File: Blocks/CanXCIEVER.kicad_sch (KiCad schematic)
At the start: 2 parts, among them IC45 TCAN337DCNR, J5 TC0203620000G

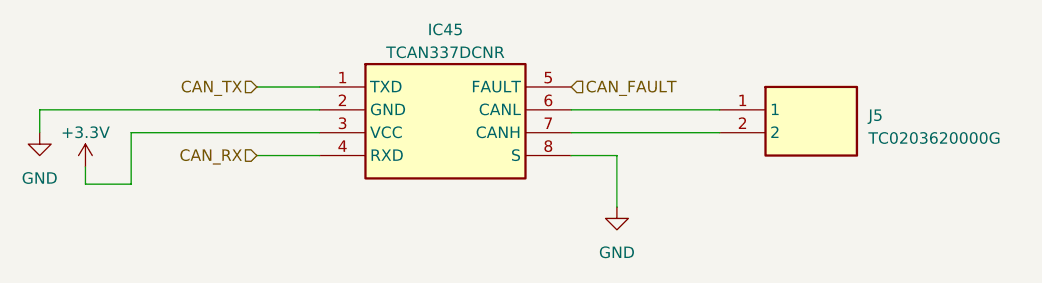
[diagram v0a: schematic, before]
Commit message: Automate library addition * Added script to automagically extract samacsys libraries and put them in corresponding folders. * Note: Requires zsh
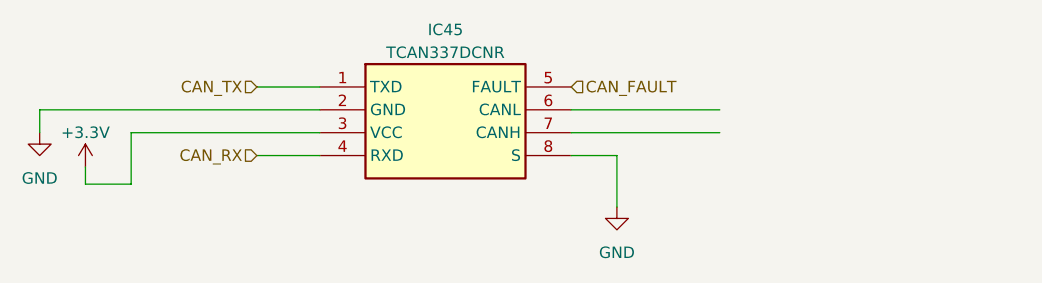
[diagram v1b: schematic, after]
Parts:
- removed J5: TC0203620000G, TC0203620000G:TC0203620000G, symbol TC0203620000G:TC0203620000G
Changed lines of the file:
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@@
   (symbol (lib_id "power:+3.3V") (at 98.425 107.95 0) (unit 1)
     (in_bom yes) (on_board yes) (dnp no) (fields_autoplaced)
-    (property "Reference" "#PWR0117" (at 98.425 111.76 0)
+    (property "Reference" "#PWR0284" (at 98.425 111.76 0)
       (effects (font (size 1.27 1.27)) hide)
     )
@@
       (project "PLC-CIM"
         (path "/98f81d77-8880-491b-a7cf-4c27e2d73edf/a733259a-e36e-4b53-aba1-6642256ff9ff"
-          (reference "#PWR0117") (unit 1)
+          (reference "#PWR0284") (unit 1)
         )
       )
@@
   (symbol (lib_id "power:GND") (at 157.48 112.395 0) (unit 1)
     (in_bom yes) (on_board yes) (dnp no) (fields_autoplaced)
-    (property "Reference" "#PWR0124" (at 157.48 118.745 0)
+    (property "Reference" "#PWR0283" (at 157.48 118.745 0)
       (effects (font (size 1.27 1.27)) hide)
     )
@@
       (project "PLC-CIM"
         (path "/98f81d77-8880-491b-a7cf-4c27e2d73edf/a733259a-e36e-4b53-aba1-6642256ff9ff"
-          (reference "#PWR0124") (unit 1)
+          (reference "#PWR0283") (unit 1)
         )
       )
@@
     )
   )
-  (symbol (lib_id "TC0203620000G:TC0203620000G") (at 168.91 101.6 0) (unit 1)
-    (in_bom yes) (on_board yes) (dnp no) (fields_autoplaced)
-    (property "Reference" "J5" (at 185.42 102.235 0)
-      (effects (font (size 1.27 1.27)) (justify left))
-    )
-    (property "Value" "TC0203620000G" (at 185.42 104.775 0)
-      (effects (font (size 1.27 1.27)) (justify left))
-    )
-    (property "Footprint" "TC0203620000G:TC0203620000G" (at 185.42 196.52 0)
-      (effects (font (size 1.27 1.27)) (justify left top) hide)
-    )
-    (property "Datasheet" "https://componentsearchengine.com/Datasheets/1/TC0203620000G.pdf" (at 185.42 296.52 0)
-      (effects (font (size 1.27 1.27)) (justify left top) hide)
-    )
-    (property "Height" "10.5" (at 185.42 496.52 0)
-      (effects (font (size 1.27 1.27)) (justify left top) hide)
-    )
-    (property "Mouser Part Number" "649-TC02036200J0G" (at 185.42 596.52 0)
-      (effects (font (size 1.27 1.27)) (justify left top) hide)
-    )
-    (property "Mouser Price/Stock" "https://www.mouser.co.uk/ProductDetail/Amphenol-Anytek/TC0203620000G?qs=Mv7BduZupUiHURQaUHJ1XQ%3D%3D" (at 185.42 696.52 0)
-      (effects (font (size 1.27 1.27)) (justify left top) hide)
-    )
-    (property "Manufacturer_Name" "Amphenol" (at 185.42 796.52 0)
-      (effects (font (size 1.27 1.27)) (justify left top) hide)
-    )
-    (property "Manufacturer_Part_Number" "TC0203620000G" (at 185.42 896.52 0)
-      (effects (font (size 1.27 1.27)) (justify left top) hide)
-    )
-    (pin "1")
-    (pin "2")
-    (instances
-      (project "PLC-CIM"
-        (path "/98f81d77-8880-491b-a7cf-4c27e2d73edf"
-          (reference "J5") (unit 1)
-        )
-        (path "/98f81d77-8880-491b-a7cf-4c27e2d73edf/65732d30-4757-4d69-a8f8-277854263560"
-          (reference "J6") (unit 1)
-        )
-        (path "/98f81d77-8880-491b-a7cf-4c27e2d73edf/a733259a-e36e-4b53-aba1-6642256ff9ff"
-          (reference "J12") (unit 1)
-        )
-      )
-    )
-  )
   (symbol (lib_id "power:GND") (at 93.345 104.14 0) (unit 1)
     (in_bom yes) (on_board yes) (dnp no) (fields_autoplaced)
-    (property "Reference" "#PWR0116" (at 93.345 110.49 0)
+    (property "Reference" "#PWR0282" (at 93.345 110.49 0)
       (effects (font (size 1.27 1.27)) hide)
     )
@@
       (project "PLC-CIM"
         (path "/98f81d77-8880-491b-a7cf-4c27e2d73edf/a733259a-e36e-4b53-aba1-6642256ff9ff"
-          (reference "#PWR0116") (unit 1)
+          (reference "#PWR0282") (unit 1)
         )
       )
